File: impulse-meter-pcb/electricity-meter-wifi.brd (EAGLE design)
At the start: 34.3 x 68.8 mm, 12 parts

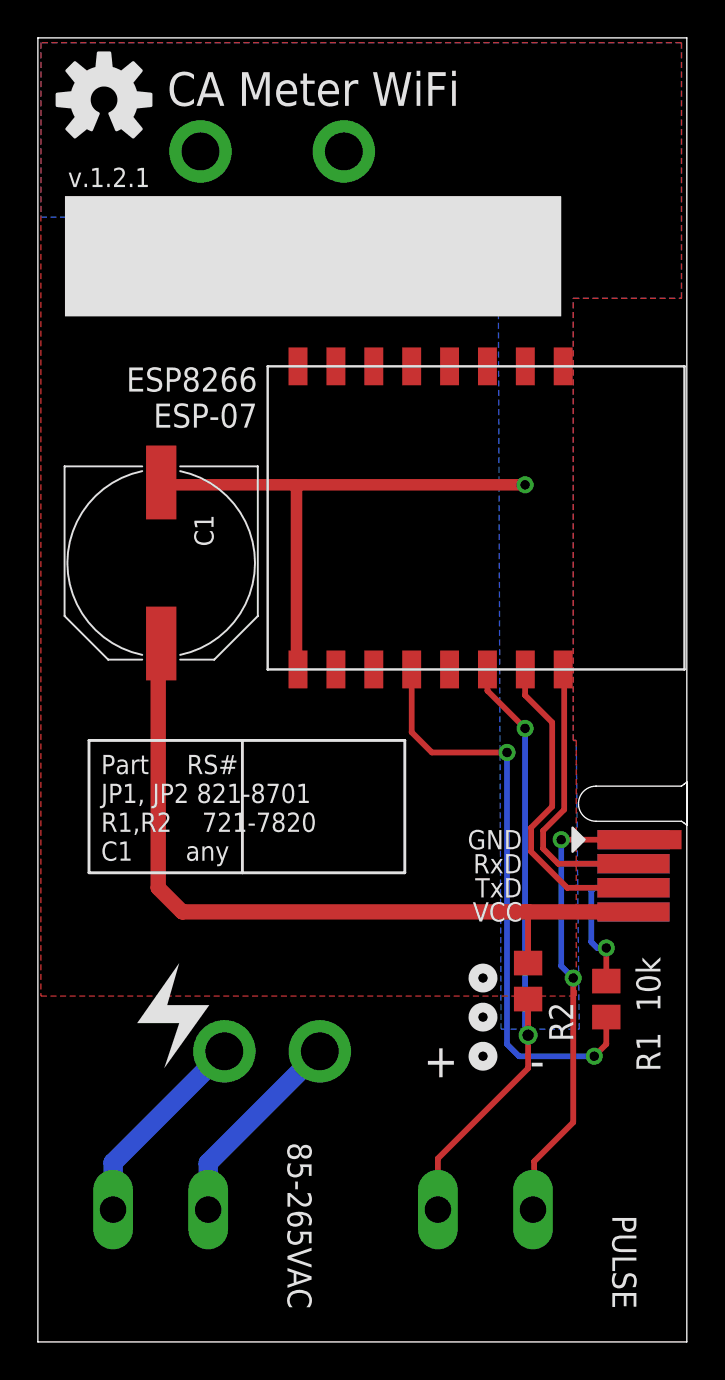
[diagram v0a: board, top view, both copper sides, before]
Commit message: added pull down on gpio 15
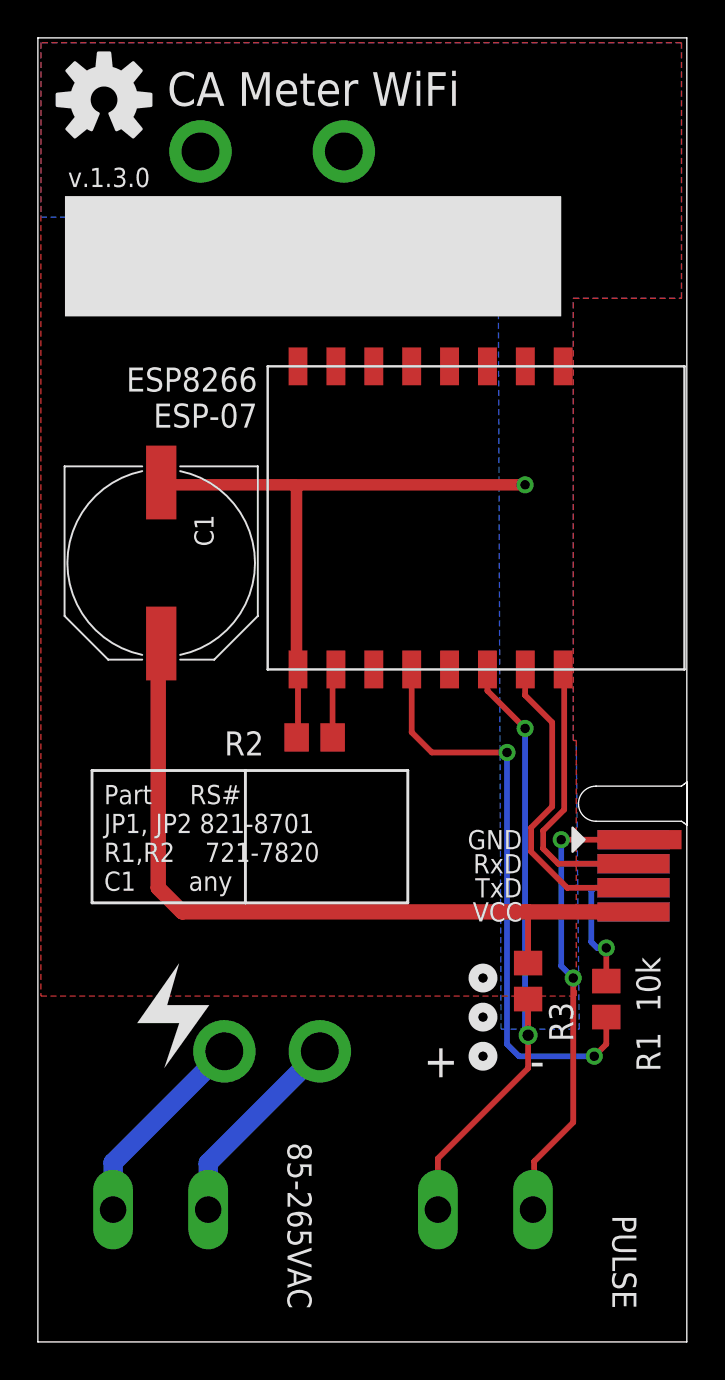
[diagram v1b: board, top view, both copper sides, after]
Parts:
- added R3: 10k, rcl:R0805
- moved R2 17.1 mm to (14.6, 31.9), turned to 0 degrees
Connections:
- new net N$7: ESP8266_ESP-07.GPIO15, R2.2
- net 3.3V: now also R3.1; no longer R2.1
- net GND: now also R2.1
- net N$3: now also R3.2; no longer R2.2
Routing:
- net N$7: track 0.00 -> 3.66 mm
- net GND: track 57.9 -> 61.5 mm
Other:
- board text added: "v.1.3.0"
- board text removed: "v.1.2.1"
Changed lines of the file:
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@@
 <text x="11.58875" y="48.26" size="1.27" layer="25" ratio="10" align="bottom-right">ESP8266
 ESP-07</text>
-<text x="1.5875" y="60.96" size="1.016" layer="25" ratio="15">v.1.2.1</text>
-<text x="3.33375" y="25.4" size="1.016" layer="25" font="fixed">Part     RS#
+<text x="1.5875" y="60.96" size="1.016" layer="25" ratio="15">v.1.3.0</text>
+<text x="3.4925" y="23.8125" size="1.016" layer="25" font="fixed">Part     RS#
 JP1, JP2 821-8701
 R1,R2    721-7820
 C1       any</text>
-<wire x1="2.69875" y1="31.75" x2="10.795" y2="31.75" width="0.1524" layer="25"/>
-<wire x1="10.795" y1="31.75" x2="19.3675" y2="31.75" width="0.1524" layer="25"/>
-<wire x1="19.3675" y1="31.75" x2="19.3675" y2="24.765" width="0.1524" layer="25"/>
-<wire x1="19.3675" y1="24.765" x2="10.795" y2="24.765" width="0.1524" layer="25"/>
-<wire x1="10.795" y1="24.765" x2="2.69875" y2="24.765" width="0.1524" layer="25"/>
-<wire x1="2.69875" y1="24.765" x2="2.69875" y2="31.75" width="0.1524" layer="25"/>
-<wire x1="10.795" y1="31.75" x2="10.795" y2="24.765" width="0.1524" layer="25"/>
+<wire x1="2.8575" y1="30.1625" x2="10.95375" y2="30.1625" width="0.1524" layer="25"/>
+<wire x1="10.95375" y1="30.1625" x2="19.52625" y2="30.1625" width="0.1524" layer="25"/>
+<wire x1="19.52625" y1="30.1625" x2="19.52625" y2="23.1775" width="0.1524" layer="25"/>
+<wire x1="19.52625" y1="23.1775" x2="10.95375" y2="23.1775" width="0.1524" layer="25"/>
+<wire x1="10.95375" y1="23.1775" x2="2.8575" y2="23.1775" width="0.1524" layer="25"/>
+<wire x1="2.8575" y1="23.1775" x2="2.8575" y2="30.1625" width="0.1524" layer="25"/>
+<wire x1="10.95375" y1="30.1625" x2="10.95375" y2="23.1775" width="0.1524" layer="25"/>
 <text x="6.82625" y="65.24625" size="1.778" layer="25" ratio="15">CA Meter WiFi</text>
 <wire x1="0.3625" y1="13.58" x2="24.3625" y2="13.58" width="0.4064" layer="26"/>
@@
 <element name="C1" library="rcl" package="PANASONIC_G" value="" x="6.50875" y="41.11625" rot="R270"/>
 <element name="U$1" library="con-pcb-slot" package="CONN_SLOT_MINIMAL" value="CON-PCB-SLOT-0.05MINIMAL" x="31.714440625" y="24.60625" smashed="yes" rot="R90"/>
-<element name="R2" library="rcl" package="R0805" value="10k" x="25.87625" y="19.05" smashed="yes" rot="R270">
+<element name="R3" library="rcl" package="R0805" value="10k" x="25.87625" y="19.05" smashed="yes" rot="R270">
 <attribute name="NAME" x="26.9875" y="17.93875" size="1.27" layer="25" rot="R270"/>
 <attribute name="VALUE" x="26.82875" y="23.1775" size="1.27" layer="27" rot="R270"/>
+</element>
+<element name="R2" library="rcl" package="R0805" value="10k" x="14.605" y="31.90875" smashed="yes">
+<attribute name="NAME" x="9.8425" y="30.95625" size="1.27" layer="25"/>
+<attribute name="VALUE" x="17.145" y="30.95625" size="1.27" layer="27"/>
 </element>
 </elements>
@@
 <wire x1="26.19375" y1="9.525" x2="28.2575" y2="11.58875" width="0.3048" layer="1"/>
 <wire x1="28.2575" y1="11.58875" x2="28.2575" y2="19.20875" width="0.3048" layer="1"/>
-<wire x1="26.19375" y1="7.045" x2="26.13375" y2="6.985" width="0" layer="19" extent="1-1"/>
+<contactref element="R2" pad="1"/>
+<wire x1="26.13375" y1="6.985" x2="26.19375" y2="7.045" width="0" layer="19" extent="1-1"/>
+<wire x1="13.73" y1="35.4975" x2="13.73" y2="31.98375" width="0.3048" layer="1"/>
+<wire x1="13.73" y1="31.98375" x2="13.655" y2="31.90875" width="0.3048" layer="1"/>
 </signal>
 <signal name="3.3V">
@@
 <wire x1="6.35" y1="23.97125" x2="7.62" y2="22.70125" width="0.8128" layer="1"/>
 <wire x1="7.62" y1="22.70125" x2="25.87625" y2="22.70125" width="0.8128" layer="1"/>
-<contactref element="R2" pad="1"/>
+<contactref element="R3" pad="1"/>
 <wire x1="25.87625" y1="22.70125" x2="31.439440625" y2="22.70125" width="0.8128" layer="1"/>
 <wire x1="25.87625" y1="22.70125" x2="25.87625" y2="20" width="0.3048" layer="1"/>
@@
 <signal name="N$3">
 <contactref element="JP2" pad="1"/>
-<contactref element="R2" pad="2"/>
+<contactref element="R3" pad="2"/>
 <contactref element="ESP8266_ESP-07" pad="GPIO4"/>
 <wire x1="23.73" y1="35.4975" x2="23.73" y2="34.3725" width="0.3048" layer="1"/>
@@
 <via x="25.87625" y="16.1925" extent="1-16" drill="0.6"/>
 </signal>
+<signal name="N$7">
+<contactref element="R2" pad="2"/>
+<contactref element="ESP8266_ESP-07" pad="GPIO15"/>
+<wire x1="15.555" y1="31.90875" x2="15.555" y2="35.3225" width="0.3048" layer="1"/>
+<wire x1="15.555" y1="35.3225" x2="15.73" y2="35.4975" width="0.3048" layer="1"/>
+</signal>
 </signals>

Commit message: pcb: v.1.3.1
added voltage supervisor MCP1316MT-29ME/OT
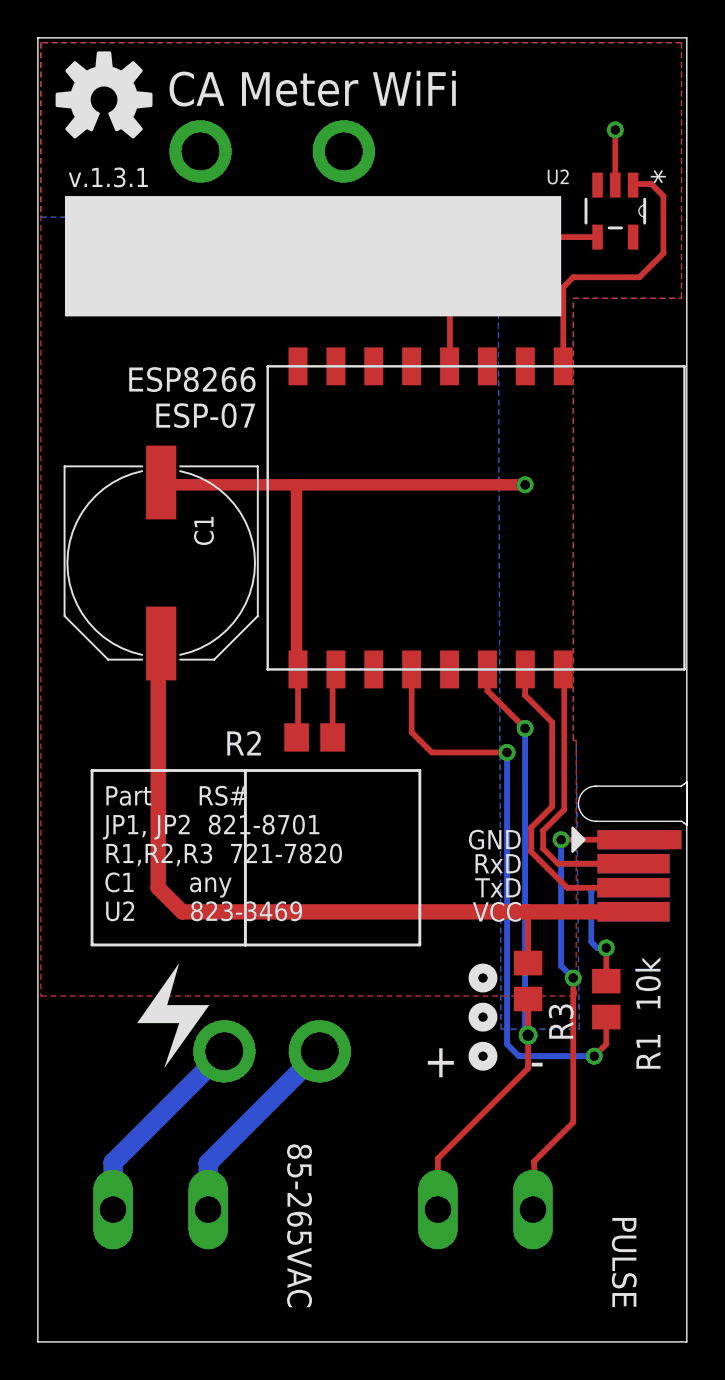
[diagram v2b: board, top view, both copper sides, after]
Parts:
- added U2: MCP1316MT-29ME/OT, Microchip_By_element14_Batch_1:SOT95P270X145-5N
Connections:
- new net N$8: ESP8266_ESP-07.REST, U2.1
- new net N$9: ESP8266_ESP-07.GPIO16, U2.4
- net 3.3V: now also U2.5
- net GND: now also U2.2
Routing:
- net N$8: track 0.00 -> 15.1 mm
- net N$9: track 0.00 -> 13.8 mm
- net GND: track 61.5 -> 64.4 mm, vias 3 -> 4
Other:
- board text added: "Part RS# JP1, JP2 821-8701 R1,R2,R3 721-7820 C1 any U2 823-3469"
- board text added: "v.1.3.1"
- board text removed: "Part RS# JP1, JP2 821-8701 R1,R2 721-7820 C1 any"
- board text removed: "v.1.3.0"
